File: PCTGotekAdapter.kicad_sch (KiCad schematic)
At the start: 21 parts, among them J1 Conn_02x17_Odd_Even, J2 Conn_2Rows-19Pins, J3 Conn_2Rows-19Pins, J4 Conn_02x17_Odd_Even, J5 Conn_01x04_Pin, J6 Conn_01x04_Pin, U1 SN74LS138N, U2 SN7407N

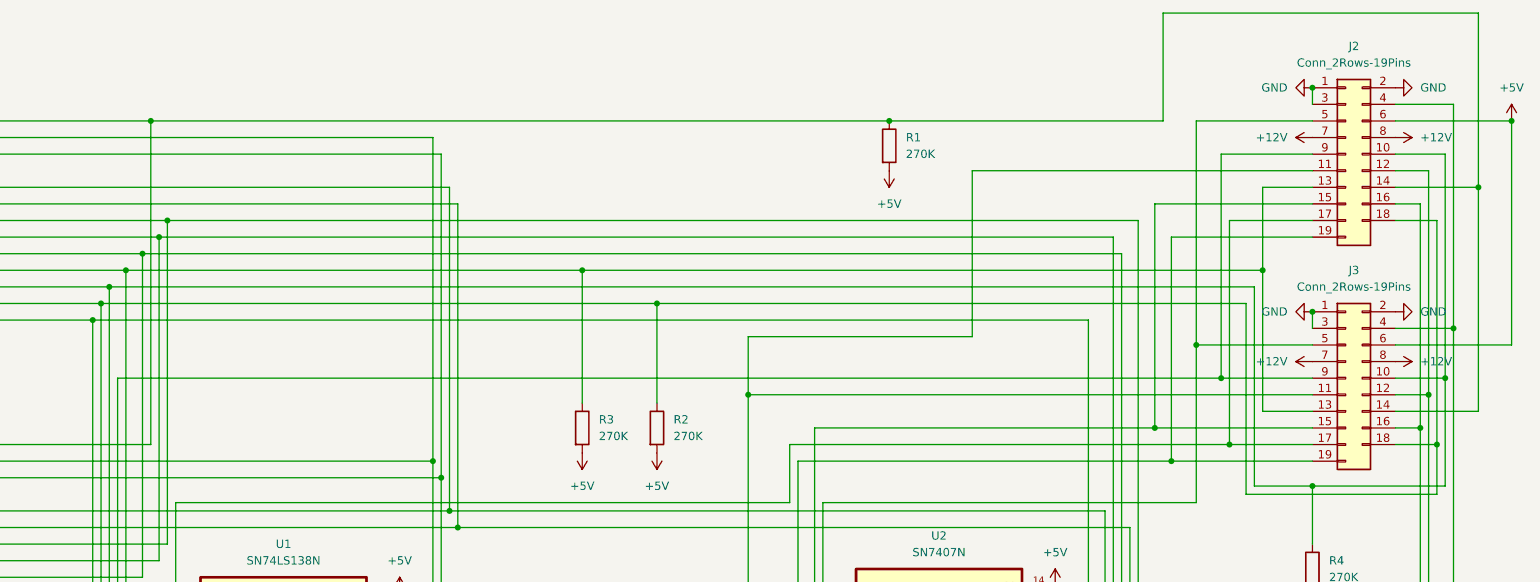
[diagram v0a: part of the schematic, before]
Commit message: Remove extraneous connector from schematic
Also some silkscreen and path tweaks
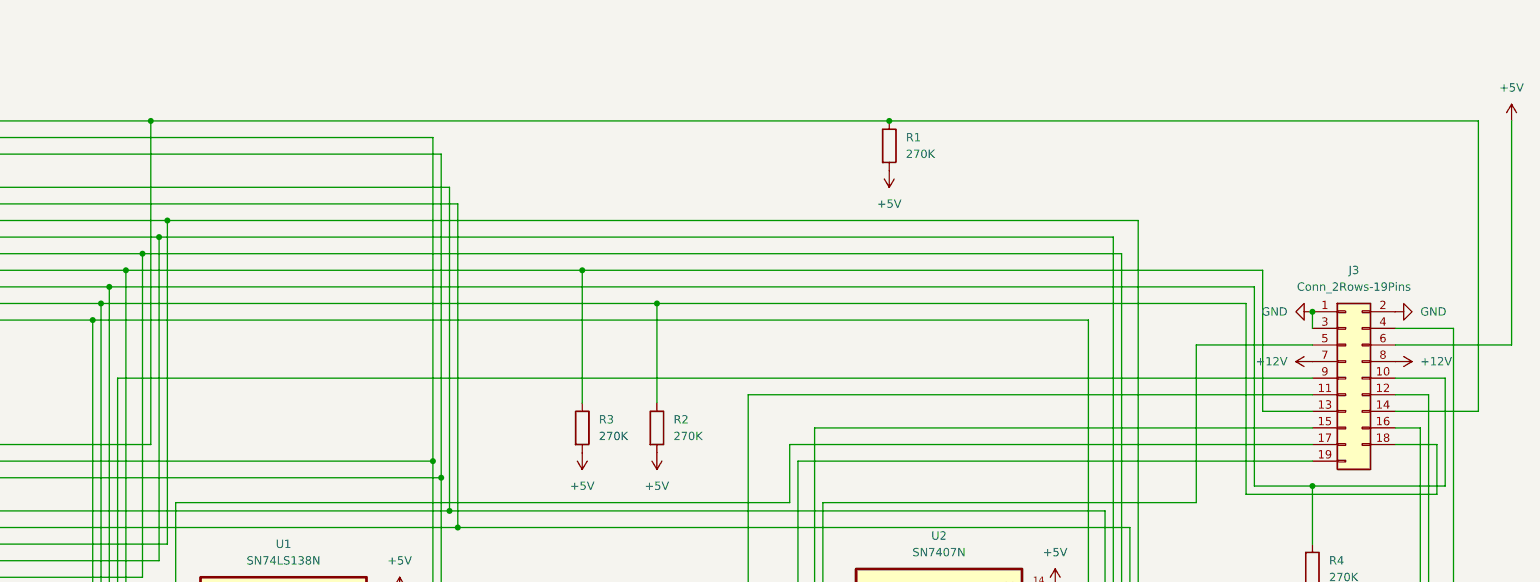
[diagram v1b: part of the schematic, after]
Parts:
- removed J2: Conn_2Rows-19Pins, Connector_PinHeader_2.54mm:PinHeader_2x10_P2.54mm_Vertical, symbol Connector_Generic:Conn_2Rows-19Pins

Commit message: Silkscreen and routing updates, schematic fixes
Also ignored .zip files
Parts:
- renumbered J3 to J2, J4 to J3
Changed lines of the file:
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@@
   (symbol (lib_id "Connector_Generic:Conn_2Rows-19Pins") (at 256.54 72.39 0) (unit 1)
     (in_bom yes) (on_board yes) (dnp no) (fields_autoplaced)
-    (property "Reference" "J3" (at 257.81 55.88 0)
+    (property "Reference" "J2" (at 257.81 55.88 0)
       (effects (font (size 1.27 1.27)))
     )
@@
       (project "PCTGotekAdapter"
         (path "/7ffcb4f6-1ab6-49c2-b08b-a8faac924e64"
-          (reference "J3") (unit 1)
+          (reference "J2") (unit 1)
         )
       )
@@
   (symbol (lib_id "Connector_Generic:Conn_02x17_Odd_Even") (at 38.1 95.25 0) (unit 1)
     (in_bom yes) (on_board yes) (dnp no) (fields_autoplaced)
-    (property "Reference" "J4" (at 39.37 68.58 0)
+    (property "Reference" "J3" (at 39.37 68.58 0)
       (effects (font (size 1.27 1.27)))
     )
@@
       (project "PCTGotekAdapter"
         (path "/7ffcb4f6-1ab6-49c2-b08b-a8faac924e64"
-          (reference "J4") (unit 1)
-        )
-      )
+          (reference "J3") (unit 1)
+        )
+      )

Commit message: Changes to schematic info
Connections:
- no-connect marks 10 -> 16
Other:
- company: Author: AJ Fite <N7AJ@ajfite.com> -> Author: AJ Fite <me@ajfite.com>
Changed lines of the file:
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@@
   (title_block
     (title "PC Transporter to MS DOS Drive Adapter")
-    (date "2023-06-04")
+    (date "2023-07-27")
     (rev "${Rev}")
-    (company "Author: AJ Fite <N7AJ@ajfite.com>")
+    (company "Author: AJ Fite <me@ajfite.com>")
+    (comment 1 "Note: There is no J4 due to changes in Rev B")
   )
   (junction (at 111.76 105.41) (diameter 0) (color 0 0 0 0)
@@
   (no_connect (at 45.72 30.48))
   (no_connect (at 45.72 80.01))
+  (no_connect (at 111.76 110.49))
+  (no_connect (at 111.76 118.11))
+  (no_connect (at 111.76 113.03))
   (no_connect (at 45.72 40.64))
+  (no_connect (at 111.76 128.27))
   (no_connect (at 45.72 77.47))
+  (no_connect (at 111.76 120.65))
   (no_connect (at 45.72 66.04))
+  (no_connect (at 111.76 115.57))
   (no_connect (at 45.72 27.94))
   (no_connect (at 45.72 115.57))

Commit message: Correct an error on the schematic
Resistors were listed as 270K, they should be 2.7K
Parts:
- R1, R2, R3, R4: value 270K -> 2.7K
